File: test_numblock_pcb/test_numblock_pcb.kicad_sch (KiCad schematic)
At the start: 21 parts, among them J1 AVR-ISP-6, J2 USB4105GFA120, SW18 SW_Push, U1 ATmega32U4-A, Y1 16MHz

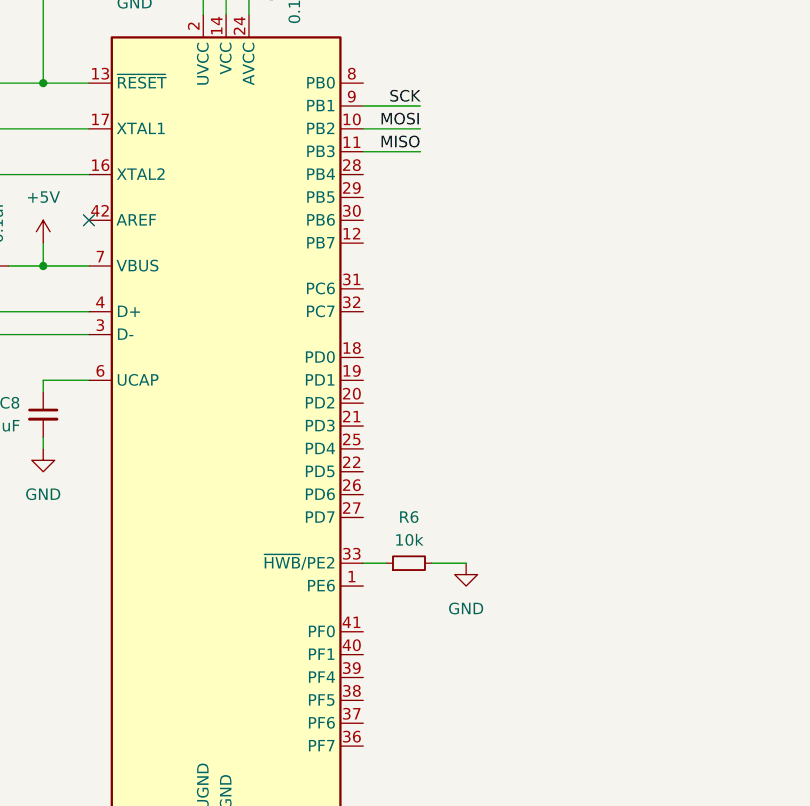
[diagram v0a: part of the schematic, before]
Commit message: complete the prototype numpad pcb
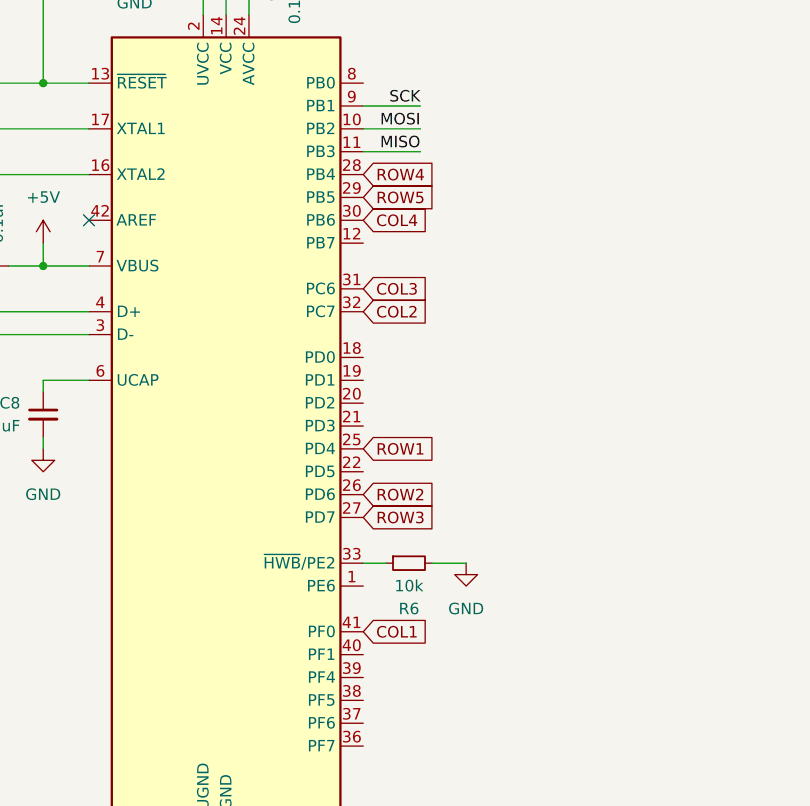
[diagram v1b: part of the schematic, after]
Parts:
- J1: footprint Connector_IDC:IDC-Header_2x03_P2.54mm_Vertical -> Connector_PinHeader_2.54mm:PinHeader_2x03_P2.54mm_Vertical
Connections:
- net ROW1: now reaches U1.25 (PD4)
- net ROW2: now reaches U1.26 (PD6)
- net ROW3: now reaches U1.27 (PD7)
- net ROW4: now reaches U1.28 (PB4)
- net ROW5: now reaches U1.29 (PB5)
- net COL4: now reaches U1.30 (PB6)
- net COL3: now reaches U1.31 (PC6)
- net COL2: now reaches U1.32 (PC7)
- net COL1: now reaches U1.41 (PF0)
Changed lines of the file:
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@@
+		)
+	)
+	(global_label "ROW1"
+		(shape input)
+		(at 113.03 119.38 0)
+		(fields_autoplaced yes)
+		(effects
+			(font
+				(size 1.27 1.27)
+			)
+			(justify left)
+		)
+		(property "Intersheetrefs" "${INTERSHEET_REFS}"
+			(at 106.7791 119.38 0)
+			(effects
+				(font
+					(size 1.27 1.27)
+				)
+				(justify right)
+				(hide yes)
+			)
+		)
+	)
+	(global_label "COL1"
+		(shape input)
+		(at 113.03 139.7 0)
+		(fields_autoplaced yes)
+		(effects
+			(font
+				(size 1.27 1.27)
+			)
+			(justify left)
+		)
+		(property "Intersheetrefs" "${INTERSHEET_REFS}"
+			(at 120.8533 139.7 0)
+			(effects
+				(font
+					(size 1.27 1.27)
+				)
+				(justify left)
+				(hide yes)
+			)
+		)
+	)
+	(global_label "COL3"
+		(shape input)
+		(at 113.03 101.6 0)
+		(fields_autoplaced yes)
+		(effects
+			(font
+				(size 1.27 1.27)
+			)
+			(justify left)
+		)
+		(property "Intersheetrefs" "${INTERSHEET_REFS}"
+			(at 120.8533 101.6 0)
+			(effects
+				(font
+					(size 1.27 1.27)
+				)
+				(justify left)
+				(hide yes)
+			)
+		)
+	)
+	(global_label "ROW2"
+		(shape input)
+		(at 113.03 124.46 0)
+		(fields_autoplaced yes)
+		(effects
+			(font
+				(size 1.27 1.27)
+			)
+			(justify left)
+		)
+		(property "Intersheetrefs" "${INTERSHEET_REFS}"
+			(at 106.7791 124.46 0)
+			(effects
+				(font
+					(size 1.27 1.27)
+				)
+				(justify right)
+				(hide yes)
+			)
+		)
+	)
+	(global_label "COL4"
+		(shape input)
+		(at 113.03 93.98 0)
+		(fields_autoplaced yes)
+		(effects
+			(font
+				(size 1.27 1.27)
+			)
+			(justify left)
+		)
+		(property "Intersheetrefs" "${INTERSHEET_REFS}"
+			(at 120.8533 93.98 0)
+			(effects
+				(font
+					(size 1.27 1.27)
+				)
+				(justify left)
+				(hide yes)
+			)
+		)
+	)
+	(global_label "COL2"
+		(shape input)
+		(at 113.03 104.14 0)
+		(fields_autoplaced yes)
+		(effects
+			(font
+				(size 1.27 1.27)
+			)
+			(justify left)
+		)
+		(property "Intersheetrefs" "${INTERSHEET_REFS}"
+			(at 120.8533 104.14 0)
+			(effects
+				(font
+					(size 1.27 1.27)
+				)
+				(justify left)
+				(hide yes)
+			)
+		)
+	)
+	(global_label "ROW3"
+		(shape input)
+		(at 113.03 127 0)
+		(fields_autoplaced yes)
+		(effects
+			(font
+				(size 1.27 1.27)
+			)
+			(justify left)
+		)
+		(property "Intersheetrefs" "${INTERSHEET_REFS}"
+			(at 106.7791 127 0)
+			(effects
+				(font
+					(size 1.27 1.27)
+				)
+				(justify right)
+				(hide yes)
+			)
+		)
+	)
+	(global_label "ROW4"
+		(shape input)
+		(at 113.03 88.9 0)
+		(fields_autoplaced yes)
+		(effects
+			(font
+				(size 1.27 1.27)
+			)
+			(justify left)
+		)
+		(property "Intersheetrefs" "${INTERSHEET_REFS}"
+			(at 106.7791 88.9 0)
+			(effects
+				(font
+					(size 1.27 1.27)
+				)
+				(justify right)
+				(hide yes)
+			)
+		)
+	)
+	(global_label "ROW5"
+		(shape input)
+		(at 113.03 91.44 0)
+		(fields_autoplaced yes)
+		(effects
+			(font
+				(size 1.27 1.27)
+			)
+			(justify left)
+		)
+		(property "Intersheetrefs" "${INTERSHEET_REFS}"
+			(at 106.7791 91.44 0)
+			(effects
+				(font
+					(size 1.27 1.27)
+				)
+				(justify right)
+				(hide yes)
+			)
 		)
 	)
@@
 			)
 		)
-		(property "Footprint" "Connector_IDC:IDC-Header_2x03_P2.54mm_Vertical"
+		(property "Footprint" "Connector_PinHeader_2.54mm:PinHeader_2x03_P2.54mm_Vertical"
 			(at 40.64 40.64 90)
 			(effects
@@
 		(lib_id "Device:R_Small")
 		(at 118.11 132.08 90)
-		(unit 1)
-		(exclude_from_sim no)
-		(in_bom yes)
-		(on_board yes)
-		(dnp no)
-		(fields_autoplaced yes)
+		(mirror x)
+		(unit 1)
+		(exclude_from_sim no)
+		(in_bom yes)
+		(on_board yes)
+		(dnp no)
 		(property "Reference" "R6"
-			(at 118.11 127 90)
+			(at 118.11 137.16 90)
 			(effects
 				(font
@@
 		)
 		(property "Value" "10k"
-			(at 118.11 129.54 90)
-			(effects
-				(font
+			(at 118.11 134.62 90)
+			(effects
+				(font
